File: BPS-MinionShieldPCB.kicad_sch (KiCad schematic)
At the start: 78 parts, among them J1 TempConn1, J2 TempConn2, J3 Conn_01x24_Female

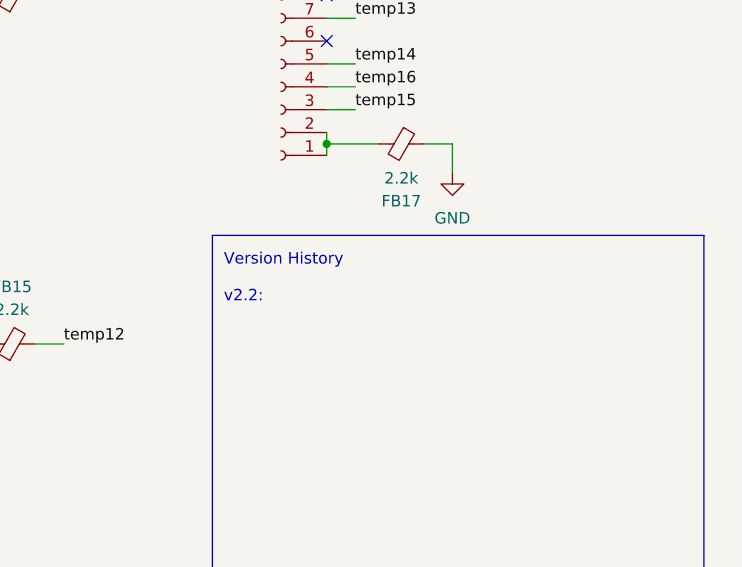
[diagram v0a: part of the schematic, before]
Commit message: Standardized common repo, added version history, updated readme, added board models
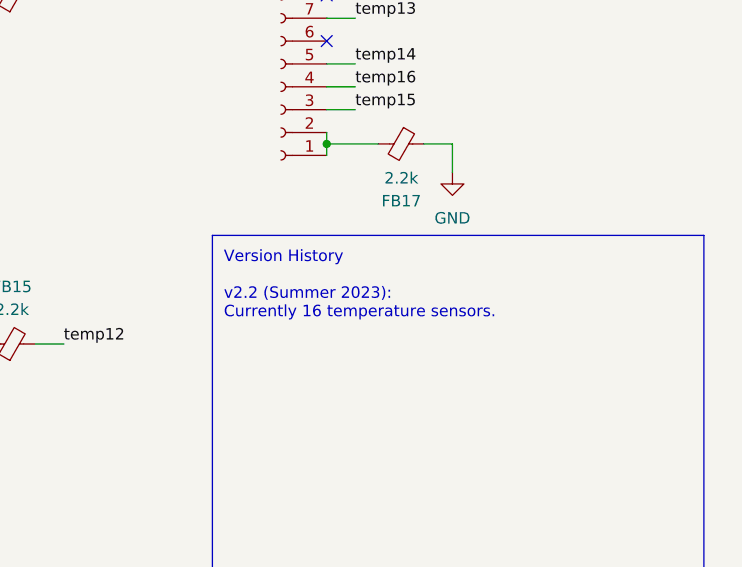
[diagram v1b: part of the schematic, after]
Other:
- note added: "Version History v2.2 (Summer 2023): Currently 16 temperature sensors."
- note removed: "Version History v2.2:"
